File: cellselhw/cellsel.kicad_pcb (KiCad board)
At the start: 2 copper layers, 59 parts, among them P1 CONN_01X04, P2 CONN_01X04, P3 CONN_01X04, P4 CONN_01X04, P5 CONN_01X08, P6 CONN_01X08, P7 CONN_01X03, P8 CONN_01X04, Q1 Q_PMOS_GDSD, Q2 Q_NMOS_GDSD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

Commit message: PCB RC1 Ready
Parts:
- added R23: 33k, Resistors_SMD:R_0603, F.Cu at (157.0, 39.0)
- added R24: 33k, Resistors_SMD:R_0603, F.Cu at (161.0, 34.2)
- P3: footprint Connectors_Molex:Molex_KK-6410-04_04x2.54mm_Straight -> Custom_Descretes:MINICON_01X04
- P7: footprint Connectors_Molex:Molex_KK-6410-03_03x2.54mm_Straight -> Custom_Descretes:DS18B20
- Q1: value Q_PMOS_GDSD -> ZXMP10A18G
- Q2: value Q_NMOS_GDSD -> FDV303N; footprint TO_SOT_Packages_SMD:SOT-223 -> TO_SOT_Packages_SMD:SOT-23
- Q3, Q4, Q5: value Q_NMOS_GDSD -> FQT4N20L
- moved P2 111.1 mm to (127.9, 17.5), turned to 270 degrees
- moved D1 101.8 mm to (137.8, 57.1), turned to 90 degrees
- moved R19 94.5 mm to (161.0, 45.0), turned to 180 degrees
- moved U8 92.2 mm to (147.0, 58.9), turned to 180 degrees
- moved R22 88.6 mm to (173.1, 62.7), turned to 90 degrees
- moved C2 81.3 mm to (138.3, 40.6), turned to 180 degrees
- moved C3 76.5 mm to (138.3, 37.8), turned to 180 degrees
- moved P8 73.5 mm to (130.8, 63.1)
- moved C4 71.3 mm to (137.9, 28.0)
- moved C15 69.4 mm to (153.8, 62.6), turned to 90 degrees
- moved R21 67.4 mm to (169.9, 62.7), turned to 270 degrees
- moved U1 65.2 mm to (135.8, 33.0), turned to 180 degrees
- moved R14 63.3 mm to (142.0, 34.7), turned to 90 degrees
- moved C12 60.0 mm to (161.0, 54.1), turned to 270 degrees
- moved C7 59.8 mm to (141.3, 45.5), turned to 0 degrees
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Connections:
- C10 pad 1: Net-(C10-Pad1) -> GND
- C11 pad 1: Net-(C10-Pad1) -> GND
- C9 pad 1: Net-(C10-Pad1) -> GND
- P3 pad 2: Net-(P3-Pad2) -> Net-(C11-Pad2)
- P3 pad 3: Net-(C11-Pad2) -> Net-(P3-Pad3)
- P3 pad 4: Net-(C10-Pad1) -> GND
- Q2 pad 2: Net-(Q1-Pad1) -> GND
- Q2 pad 3: GND -> Net-(Q1-Pad1)
- U4 pad 13: RS485TXEN -> Net-(U4-Pad13)
- U4 pad 14: RS485RXEN -> Net-(U4-Pad14)
- U4 pad 19: SWGNDEN -> Net-(U4-Pad19)
- U4 pad 2: Net-(U4-Pad2) -> RS485TXEN
- U4 pad 20: SW5VEN -> Net-(U4-Pad20)
- U4 pad 25: Net-(P3-Pad2) -> Net-(P3-Pad3)
- U4 pad 28: Net-(C10-Pad1) -> GND
- U4 pad 5: Net-(U4-Pad5) -> RS485RXEN
- U4 pad 8: Net-(U4-Pad8) -> SW5VEN
- U4 pad 9: Net-(U4-Pad9) -> SWGNDEN
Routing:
- net GND: track 77.5 -> 530.4 mm, vias 0 -> 9
- net 3V3: track 5.65 -> 145.6 mm, vias 0 -> 6
- net SW5VEN: track 0.00 -> 36.7 mm, vias 0 -> 2
- net 12V: track 122.3 -> 157.4 mm
- net IOEXRST: track 0.00 -> 32.5 mm
- net Net-(Q1-Pad2): track 4.50 -> 36.8 mm, vias 0 -> 2
- net DISCH_BUSA: track 0.00 -> 30.1 mm
- net Net-(C14-Pad1): track 0.00 -> 28.3 mm
- net UCA0RXD: track 0.00 -> 22.6 mm
- net SWGNDEN: track 0.00 -> 21.9 mm
- net DISCH_BUSB: track 0.00 -> 20.7 mm
- net UCA0TXD: track 0.00 -> 17.8 mm
- net RS485RXEN: track 0.00 -> 17.5 mm, vias 0 -> 2
- net RS485TXEN: track 0.00 -> 17.2 mm, vias 0 -> 2
- net UCB0SCL: track 45.4 -> 62.0 mm
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- added copper zone on B.Cu, net GND

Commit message: Final Production Ready Prototype
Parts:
- added P9: CONN_01X04, Connectors_Molex:Molex_KK-6410-04_04x2.54mm_Straight, F.Cu at (128.0, 43.5)
- moved R14 1.61 mm to (141.8, 33.1)
- moved R11 1.41 mm to (141.8, 35.9)
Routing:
- net GND: track 530.4 -> 552.9 mm, vias 9 -> 10
- net 12V: track 157.4 -> 178.9 mm
- net 3V3: track 145.6 -> 159.4 mm, vias 6 -> 7
- net Net-(P6-Pad8): track 0.00 -> 5.98 mm
- net Net-(P6-Pad7): track 0.00 -> 5.98 mm
- net Net-(P6-Pad6): track 0.00 -> 5.98 mm
- net Net-(P6-Pad5): track 0.00 -> 5.98 mm
- net Net-(P6-Pad4): track 0.00 -> 5.98 mm
- net Net-(P6-Pad3): track 0.00 -> 5.98 mm
- net Net-(P6-Pad2): track 0.00 -> 5.98 mm
- net Net-(P6-Pad1): track 0.00 -> 5.98 mm
- net Net-(P5-Pad8): track 0.00 -> 5.98 mm
- net Net-(P5-Pad7): track 0.00 -> 5.98 mm
- net Net-(P5-Pad6): track 0.00 -> 5.98 mm
- net Net-(P5-Pad5): track 0.00 -> 5.98 mm
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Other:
- board outline added: 81 x 54 mm

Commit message: Minor last-minute refinements
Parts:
- moved C6 1.60 mm to (136.7, 43.3)
- moved C7 0.91 mm to (142.2, 45.4)
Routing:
- net SW5VEN: track 36.9 -> 46.8 mm
- net GND: track 552.9 -> 562.5 mm
- net 3V3: track 159.4 -> 158.7 mm

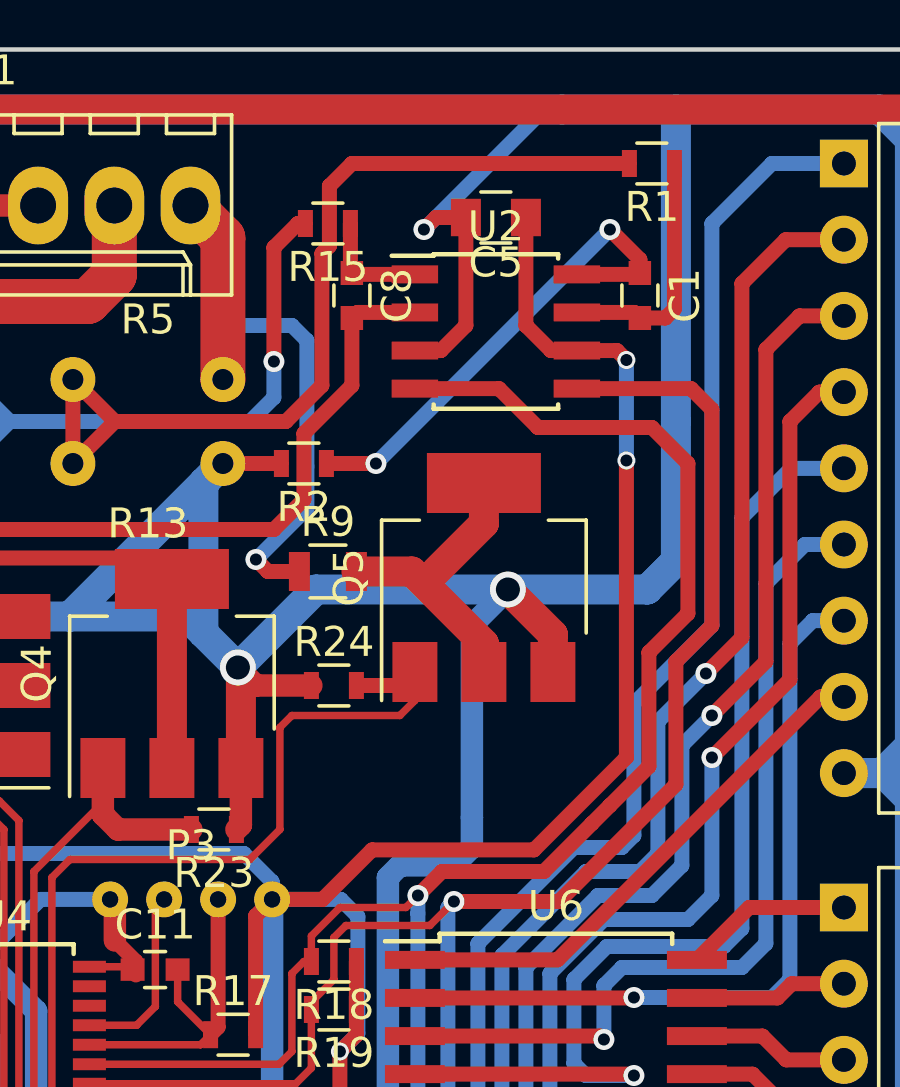
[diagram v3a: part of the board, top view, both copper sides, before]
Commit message: Connected Power Incorrectly on ADC
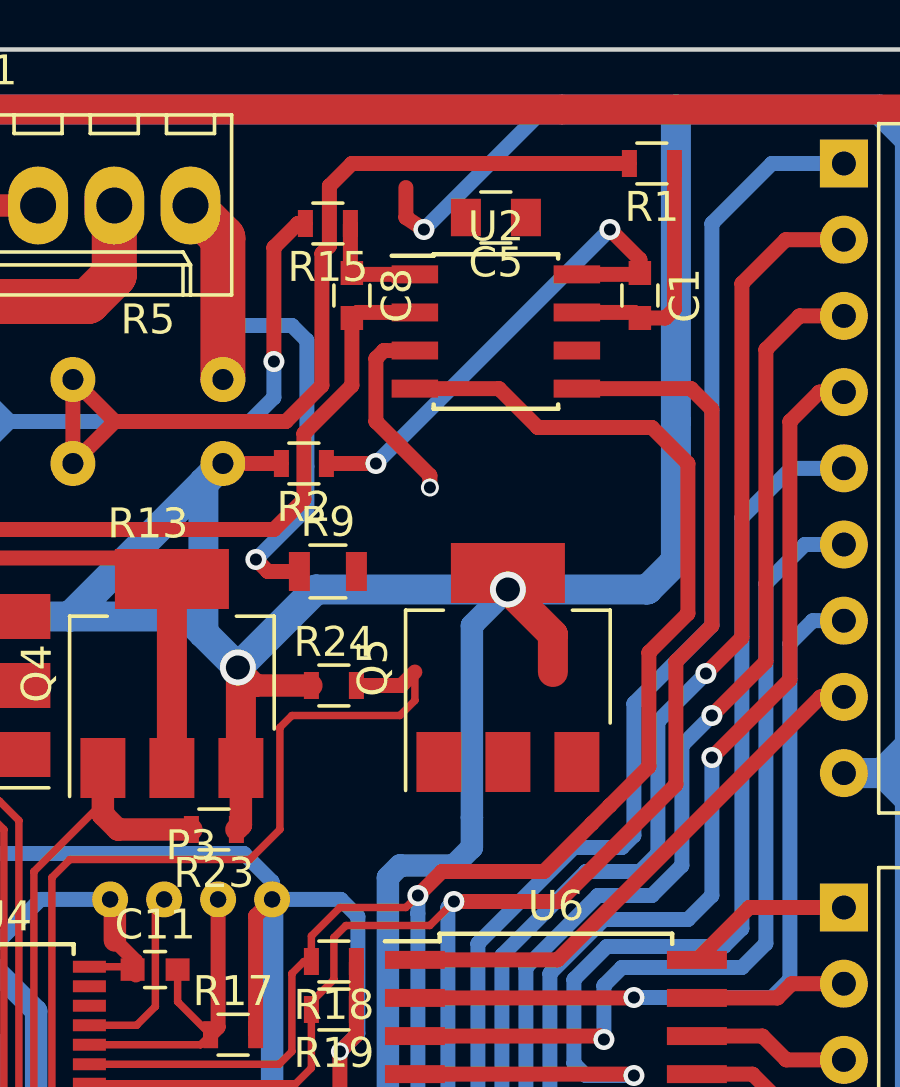
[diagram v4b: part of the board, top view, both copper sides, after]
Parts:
- R21, R22: value 10k -> 33k
- moved Q5 3.10 mm to (166.8, 33.6)
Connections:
- C5 pad 1: 3V3 -> GND
- C5 pad 2: GND -> 3V3
- U2 pad 3: GND -> 3V3
- U2 pad 6: 3V3 -> GND
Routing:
- net 3V3: track 158.7 -> 130.8 mm, vias 7 -> 6
- net Net-(Q5-Pad2): track 14.7 -> 3.37 mm, vias 0 -> 1
- net GND: track 562.5 -> 553.7 mm, vias 10 -> 9
